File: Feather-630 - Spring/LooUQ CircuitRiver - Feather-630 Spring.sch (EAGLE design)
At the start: 22 parts, among them J1 FEATHERHOST-S, J2 FEATHERHOST-L, J3 HA-CTA_HEADER, J4 JST_PH-2_T/H, J5 JST_PH-2_T/H, P1 NO MOUNT, P2 NO MOUNT, P3 BREAKOUTPAD, U2 LM2674_BUCK

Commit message: Updates for Feather-630
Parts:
- removed P1, P2: NO MOUNT, common:BREAKOUTPAD
- added J6: QWIIC_VERTICAL, common:QWIIC_VERTICAL
- added J7: B8B-PH-K-S(LF)(SN), common:B8B-PH-K-S(LF)(SN)
- added J8: DNF, common:2PIN_T/H_HEADER
- J3: value HA-CTA_HEADER -> CR-SPRING_HEADER; device common:HA-CTA_HEADER -> common:CR-SPRING_HEADER
- P3: value BREAKOUTPAD -> SLEEP; device common:BREAKOUTPAD -> common:SLEEP
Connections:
- removed net Net_17: J2.+3V3, J2.AREF, P1.1, P2.1
- removed net Net_GND: C1.MINUS, C2.MINUS, C4.2, D1.A, J2.GND@2, J3.GND, J4.P2, J5.P2, R2.2, R3.1, U2.GND
- new net Net_11: J2.A0, J7.P8
- new net Net_23: J2.A3, J7.P5
- new net Net_24: J2.A2, J7.P6
- new net Net_25: J2.A1, J7.P7
- new net Net_27: J1.SDA, J6.SDA
- new net Net_28: J1.SCI, J6.SCL
- new net Net_29: J2.+3V3, J6.3v3, J8.P1
- new net Net_VIn: C1.PLUS, J5.P1, R1.2, U2.VIN
- net Net_13: now also C1.MINUS, C2.MINUS, C4.2, D1.A, J2.GND@2, J3.GND, J4.P2, J5.P2, J6.GND, J7.P2, J8.P2, R2.2, R3.1, U2.GND; no longer C1.PLUS, J5.P1, R1.2, U2.VIN
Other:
- note added: "D9 (aka A7) is tied to Adafruit's"
- note added: "Feather vbatt sense voltage divider"
- note added: "I/O"
- note added: "JST-PH DNF"
- note removed: "D9 (aka A7) is tied to Feather"
- note removed: "vbatt sense voltage divider"
- moved on the sheet: J1, J2

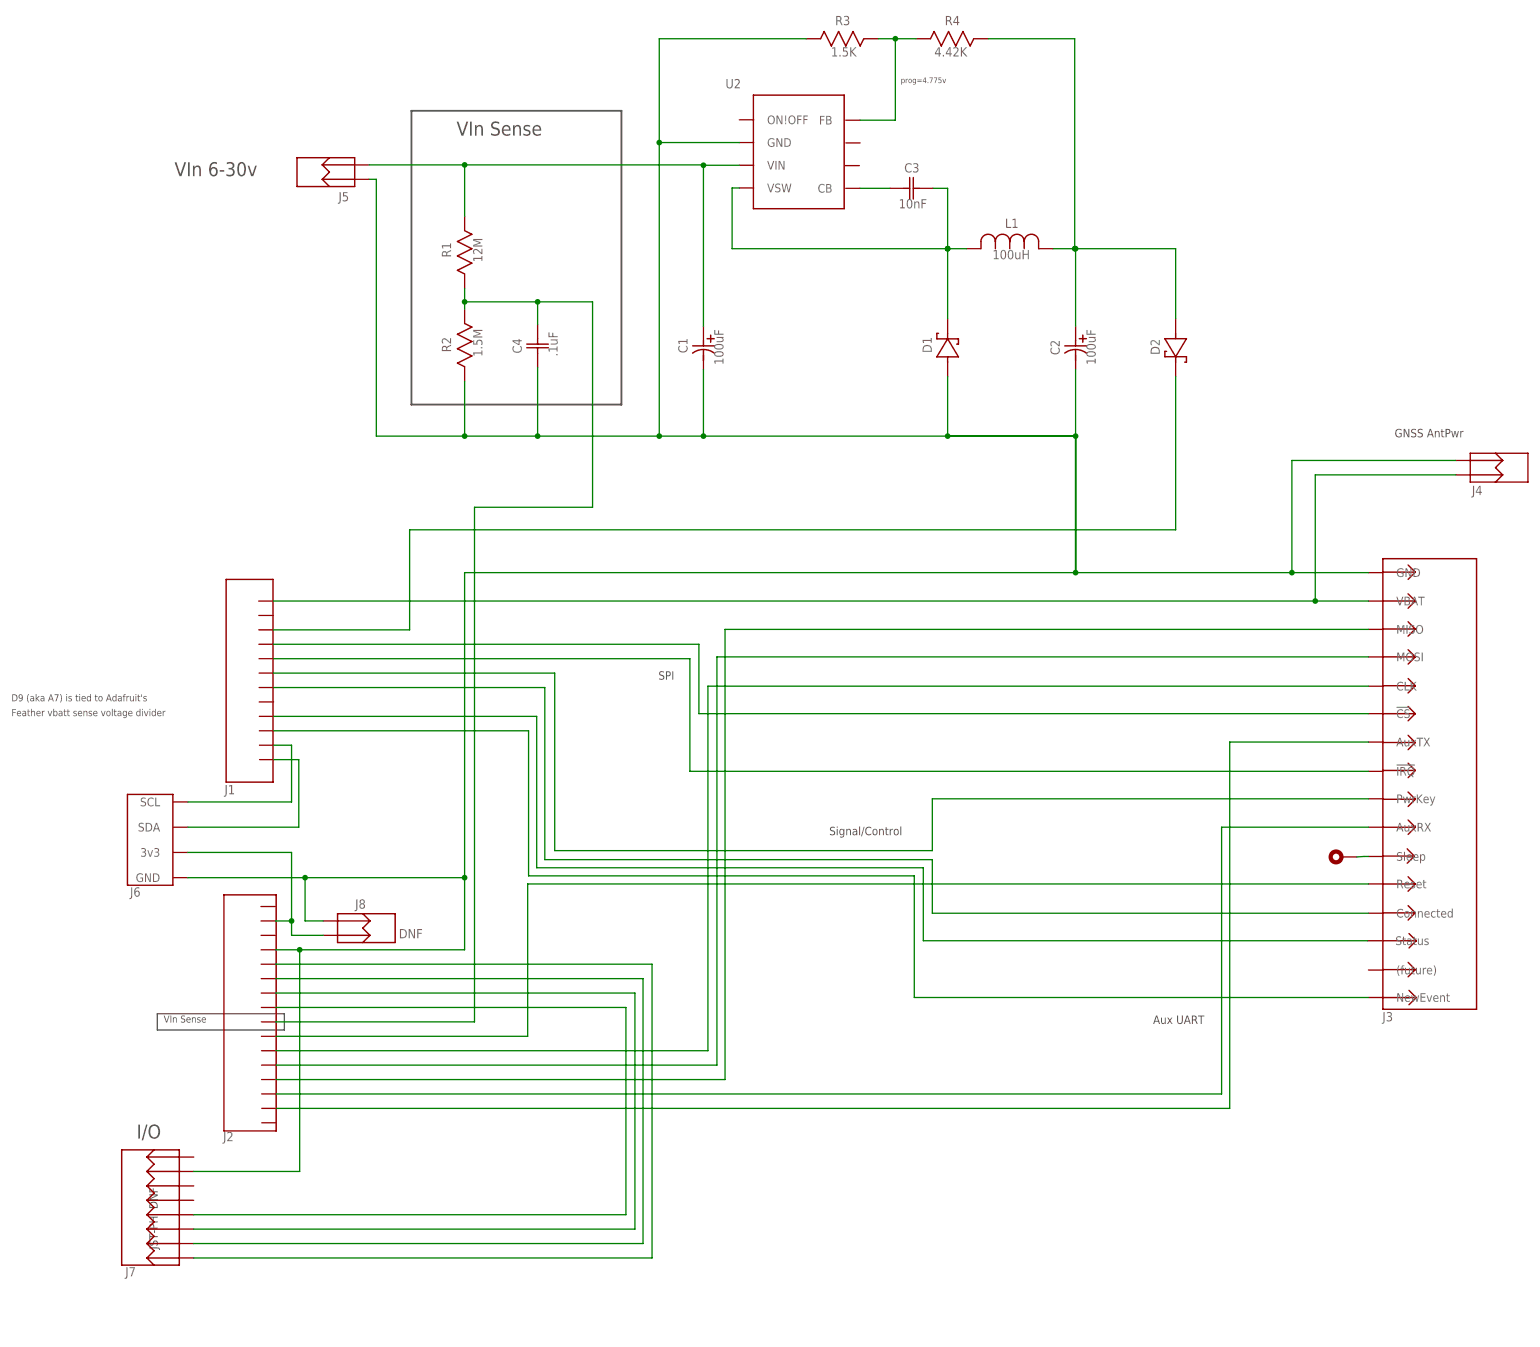
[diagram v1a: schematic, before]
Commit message: updated with CircuitRiver RapidsIO connector
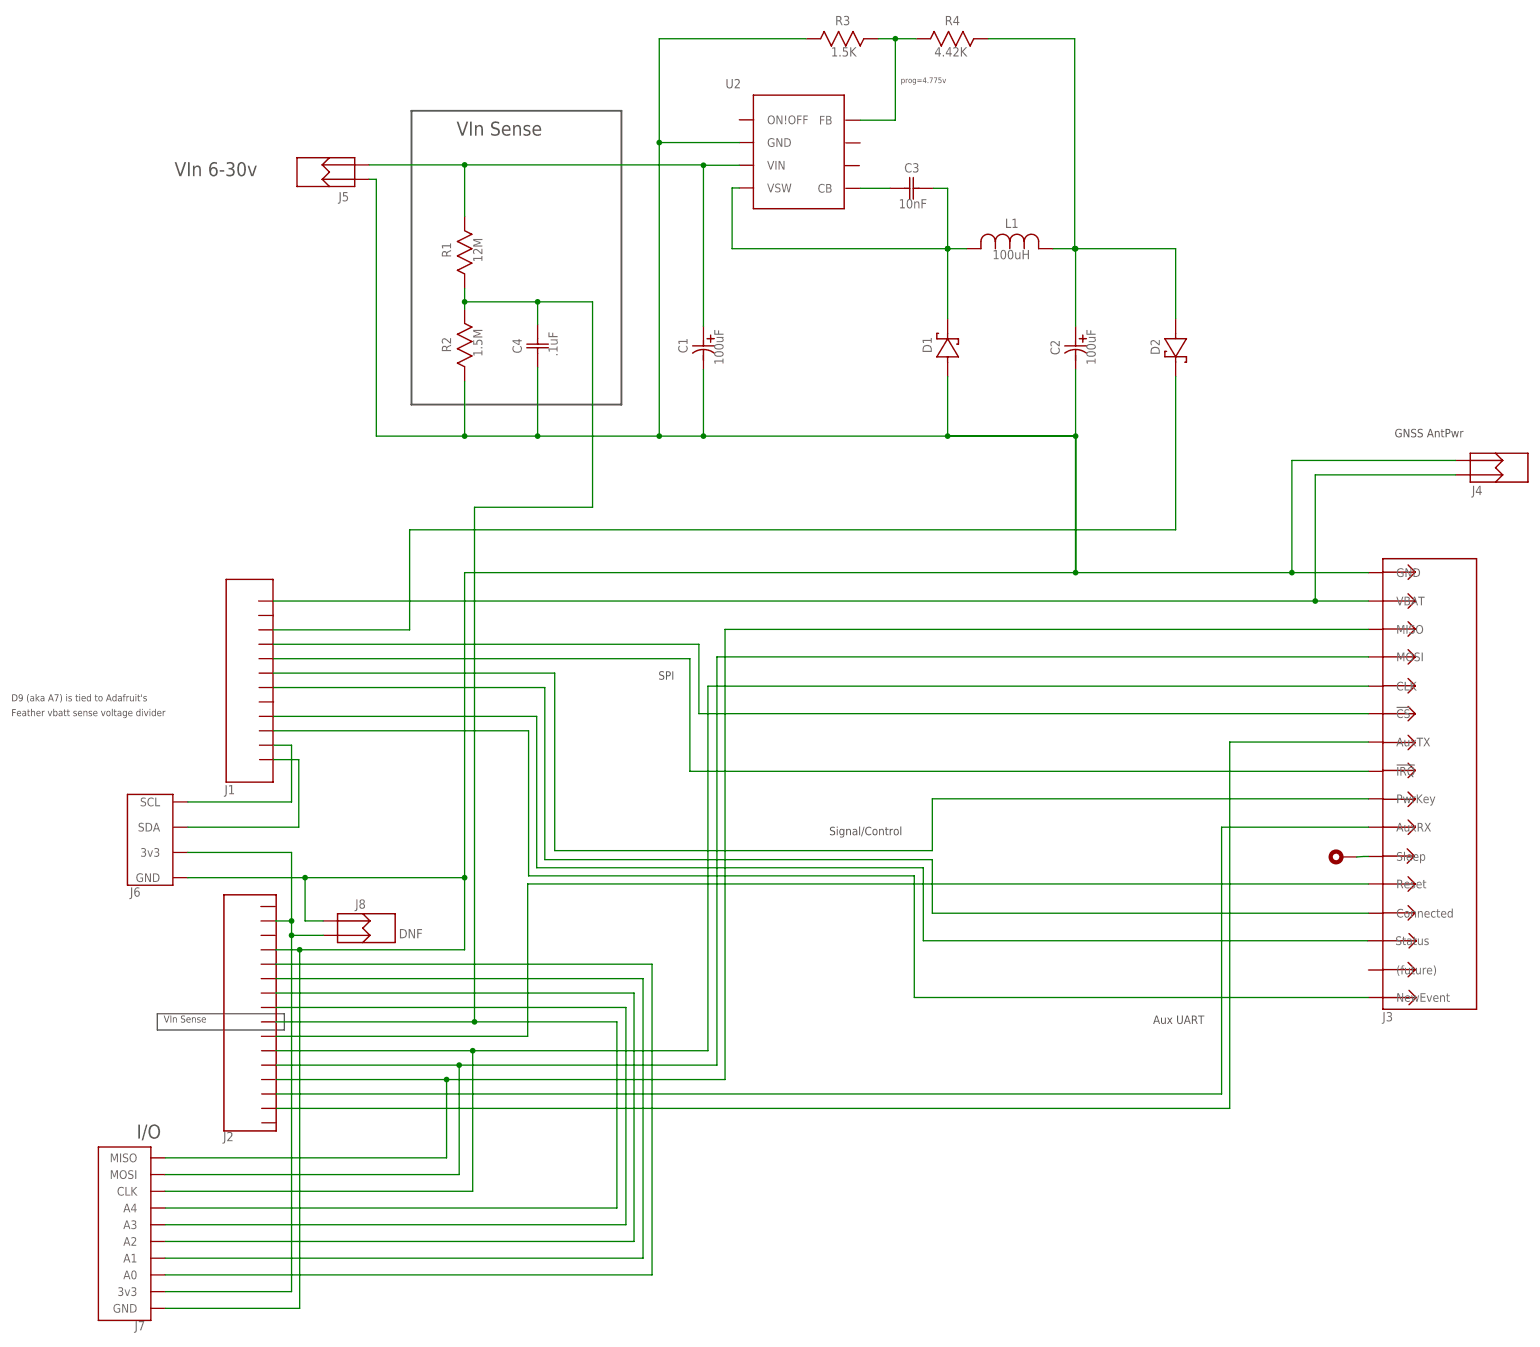
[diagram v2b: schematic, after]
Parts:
- J7: value B8B-PH-K-S(LF)(SN) -> CR-RAPIDSIO_VERTICAL; device common:B8B-PH-K-S(LF)(SN) -> common:CR-RAPIDSIO_VERTICAL
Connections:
- net Net_0 renamed Net_VBUS
- net Net_3 renamed Net_VSW
- removed net Net_13: C1.MINUS, C2.MINUS, C4.2, D1.A, J2.GND@2, J3.GND, J4.P2, J5.P2, J6.GND, J7.P2, J8.P2, R2.2, R3.1, U2.GND
- removed net Net_24: J2.A2, J7.P6
- removed net Net_29: J2.+3V3, J6.3v3, J8.P1
- new net Net_15: J2.A2, J7.A2
- new net Net_3v3: J2.+3V3, J6.3v3, J7.3v3, J8.P1
- new net Net_GND: C1.MINUS, C2.MINUS, C4.2, D1.A, J2.GND@2, J3.GND, J4.P2, J5.P2, J6.GND, J7.GND, J8.P2, R2.2, R3.1, U2.GND
- net Net_11: now also J7.A0; no longer J7.P8
- net Net_18: now also J7.A4
- net Net_2: now also J7.MISO
- net Net_23: now also J7.A3; no longer J7.P5
- net Net_25: now also J7.A1; no longer J7.P7
- net Net_6: now also J7.CLK
- net Net_8: now also J7.MOSI
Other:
- note removed: "JST-PH DNF"

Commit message: Updated Feathers
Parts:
- added P1, P2: DNF, common:DNF
- P3: value SLEEP -> DNF; device common:SLEEP -> common:DNF
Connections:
- new net Net_29: J2.AREF, J8.P1
- new net Net_30: J2.!RESET, P1.1
- net Net_3v3: now also J8.P2; no longer J8.P1
- net Net_GND: now also P2.1; no longer J8.P2
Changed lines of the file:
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@@
 <part name="LG1" library="common" deviceset="LOOUQ_LOGO" device=""/>
 <part name="LG2" library="common" deviceset="CIRCUITRIVER_LOGO" device=""/>
-<part name="P3" library="common" deviceset="SLEEP" device=""/>
+<part name="P1" library="common" deviceset="DNF" device=""/>
+<part name="P2" library="common" deviceset="DNF" device=""/>
+<part name="P3" library="common" deviceset="DNF" device=""/>
 <part name="R1" library="common" deviceset="RES_0603" device="" value="12M"/>
 <part name="R2" library="common" deviceset="RES_0603" device="" value="1.5M"/>
@@
 <instance part="LG1" gate="PART_1" x="114.776" y="131.128"/>
 <instance part="LG2" gate="PART_1" x="115.24" y="125.093"/>
+<instance part="P1" gate="BRKOUTPAD" x="-57.229" y="-13.176" rot="R90"/>
+<instance part="P2" gate="BRKOUTPAD" x="-57.071" y="-85.566" rot="R90"/>
 <instance part="P3" gate="BRKOUTPAD" x="101.362" y="-6.033" rot="R270"/>
 <instance part="R1" gate="PART_1" x="-52.223" y="100.477" rot="R90">
@@
 <busses/>
 <nets>
-<net name="Net_VBUS" class="1">
-<segment>
-<wire layer="91" width="0.25" x1="73.028" y1="78.581" x2="73.028" y2="51.594"/>
-<wire layer="91" width="0.25" x1="73.028" y1="51.594" x2="-61.913" y2="51.594"/>
-<wire layer="91" width="0.25" x1="-61.913" y1="51.594" x2="-61.913" y2="33.969"/>
-<wire layer="91" width="0.25" x1="-61.913" y1="33.969" x2="-85.94" y2="33.969"/>
-<pinref part="D2" gate="PART_1" pin="C"/>
-<pinref part="J1" gate="PART_1" pin="VBUS"/>
-</segment>
-</net>
 <net name="Net_1" class="0">
 <segment>
@@
 <pinref part="J7" gate="PART_1" pin="MISO"/>
 <junction x="-55.404" y="-45.248"/>
-</segment>
-</net>
-<net name="Net_VSW" class="1">
-<segment>
-<wire layer="91" width="0.25" x1="32.861" y1="88.741" x2="32.861" y2="101.113"/>
-<wire layer="91" width="0.25" x1="32.861" y1="101.113" x2="36.189" y2="101.113"/>
-<pinref part="D1" gate="PART_1" pin="C"/>
-<pinref part="L1" gate="PART_1" pin="1"/>
-<wire layer="91" width="0.25" x1="-5.106" y1="111.81" x2="-3.836" y2="111.81"/>
-<wire layer="91" width="0.25" x1="-5.106" y1="111.81" x2="-5.106" y2="101.113"/>
-<wire layer="91" width="0.25" x1="-5.106" y1="101.113" x2="32.861" y2="101.113"/>
-<pinref part="U2" gate="PART_1" pin="VSW"/>
-<junction x="32.861" y="101.113"/>
-<wire layer="91" width="0.25" x1="30.318" y1="111.748" x2="32.861" y2="111.748"/>
-<wire layer="91" width="0.25" x1="32.861" y1="111.748" x2="32.861" y2="101.113"/>
-<pinref part="C3" gate="PART_1" pin="2"/>
-<junction x="32.861" y="101.113"/>
 </segment>
 </net>
@@
 </segment>
 </net>
+<net name="Net_29" class="0">
+<segment>
+<wire layer="91" width="0.25" x1="-78.423" y1="-19.848" x2="-77.153" y2="-19.844"/>
+<wire layer="91" width="0.25" x1="-78.423" y1="-19.848" x2="-85.552" y2="-19.848"/>
+<pinref part="J8" gate="PART_1" pin="P1"/>
+<pinref part="J2" gate="PART_1" pin="AREF"/>
+</segment>
+</net>
+<net name="Net_30" class="0">
+<segment>
+<wire layer="91" width="0.25" x1="-60.801" y1="-13.176" x2="-80.804" y2="-13.176"/>
+<wire layer="91" width="0.25" x1="-80.804" y1="-13.176" x2="-80.804" y2="-14.768"/>
+<wire layer="91" width="0.25" x1="-80.804" y1="-14.768" x2="-85.573" y2="-14.768"/>
+<pinref part="P1" gate="BRKOUTPAD" pin="1"/>
+<pinref part="J2" gate="PART_1" pin="!RESET"/>
+</segment>
+</net>
 <net name="Net_3v3" class="1">
 <segment>
-<wire layer="91" width="0.25" x1="-77.153" y1="-19.844" x2="-82.709" y2="-19.844"/>
-<wire layer="91" width="0.25" x1="-82.709" y1="-19.844" x2="-82.709" y2="-17.308"/>
+<wire layer="91" width="0.25" x1="-100.965" y1="-5.239" x2="-82.709" y2="-5.239"/>
+<wire layer="91" width="0.25" x1="-82.709" y1="-17.304" x2="-82.709" y2="-17.308"/>
+<wire layer="91" width="0.25" x1="-82.709" y1="-5.239" x2="-82.709" y2="-17.304"/>
 <wire layer="91" width="0.25" x1="-82.709" y1="-17.308" x2="-85.563" y2="-17.308"/>
-<pinref part="J8" gate="PART_1" pin="P1"/>
+<pinref part="J6" gate="PART_1" pin="3v3"/>
 <pinref part="J2" gate="PART_1" pin="+3V3"/>
-<wire layer="91" width="0.25" x1="-100.965" y1="-5.239" x2="-82.709" y2="-5.239"/>
-<wire layer="91" width="0.25" x1="-82.709" y1="-5.239" x2="-82.709" y2="-17.308"/>
-<pinref part="J6" gate="PART_1" pin="3v3"/>
-<junction x="-82.709" y="-17.308"/>
-<wire layer="91" width="0.25" x1="-82.709" y1="-19.844" x2="-82.709" y2="-82.605"/>
+<wire layer="91" width="0.25" x1="-82.709" y1="-17.308" x2="-82.709" y2="-82.605"/>
 <wire layer="91" width="0.25" x1="-82.709" y1="-82.605" x2="-104.989" y2="-82.605"/>
 <pinref part="J7" gate="PART_1" pin="3v3"/>
-<junction x="-82.709" y="-19.844"/>
+<junction x="-82.709" y="-17.308"/>
+<wire layer="91" width="0.25" x1="-77.153" y1="-17.304" x2="-82.709" y2="-17.304"/>
+<pinref part="J8" gate="PART_1" pin="P2"/>
+<junction x="-82.709" y="-17.304"/>
 </segment>
 </net>
@@
 <pinref part="J4" gate="PART_1" pin="P2"/>
 <junction x="93.504" y="44.05"/>
-<wire layer="91" width="0.25" x1="-100.965" y1="-9.684" x2="-80.327" y2="-9.684"/>
-<wire layer="91" width="0.25" x1="-80.327" y1="-9.684" x2="-52.229" y2="-9.684"/>
+<wire layer="91" width="0.25" x1="-100.965" y1="-9.684" x2="-52.229" y2="-9.684"/>
 <pinref part="J6" gate="PART_1" pin="GND"/>
 <junction x="-52.229" y="-9.684"/>
-<wire layer="91" width="0.25" x1="-77.153" y1="-17.304" x2="-80.327" y2="-17.304"/>
-<wire layer="91" width="0.25" x1="-80.327" y1="-17.304" x2="-80.327" y2="-9.684"/>
-<pinref part="J8" gate="PART_1" pin="P2"/>
-<junction x="-80.327" y="-9.684"/>
 <wire layer="91" width="0.25" x1="-81.28" y1="-22.388" x2="-81.28" y2="-85.551"/>
 <wire layer="91" width="0.25" x1="-81.28" y1="-85.551" x2="-104.989" y2="-85.551"/>
 <pinref part="J7" gate="PART_1" pin="GND"/>
 <junction x="-81.28" y="-22.388"/>
+<wire layer="91" width="0.25" x1="-61.912" y1="-85.551" x2="-60.643" y2="-85.566"/>
+<wire layer="91" width="0.25" x1="-61.912" y1="-85.551" x2="-81.28" y2="-85.551"/>
+<pinref part="P2" gate="BRKOUTPAD" pin="1"/>
+<junction x="-81.28" y="-85.551"/>
 </segment>
 </net>
@@
 <pinref part="J4" gate="PART_1" pin="P1"/>
 <junction x="97.621" y="39.048"/>
+</segment>
+</net>
+<net name="Net_VBUS" class="1">
+<segment>
+<wire layer="91" width="0.25" x1="73.028" y1="78.581" x2="73.028" y2="51.594"/>
+<wire layer="91" width="0.25" x1="73.028" y1="51.594" x2="-61.913" y2="51.594"/>
+<wire layer="91" width="0.25" x1="-61.913" y1="51.594" x2="-61.913" y2="33.969"/>
+<wire layer="91" width="0.25" x1="-61.913" y1="33.969" x2="-85.94" y2="33.969"/>
+<pinref part="D2" gate="PART_1" pin="C"/>
+<pinref part="J1" gate="PART_1" pin="VBUS"/>
 </segment>
 </net>
@@
 </segment>
 </net>
+<net name="Net_VSW" class="1">
+<segment>
+<wire layer="91" width="0.25" x1="32.861" y1="88.741" x2="32.861" y2="101.113"/>
+<wire layer="91" width="0.25" x1="32.861" y1="101.113" x2="36.189" y2="101.113"/>
+<pinref part="D1" gate="PART_1" pin="C"/>
+<pinref part="L1" gate="PART_1" pin="1"/>
+<wire layer="91" width="0.25" x1="-5.106" y1="111.81" x2="-3.836" y2="111.81"/>
+<wire layer="91" width="0.25" x1="-5.106" y1="111.81" x2="-5.106" y2="101.113"/>
+<wire layer="91" width="0.25" x1="-5.106" y1="101.113" x2="32.861" y2="101.113"/>
+<pinref part="U2" gate="PART_1" pin="VSW"/>
+<junction x="32.861" y="101.113"/>
+<wire layer="91" width="0.25" x1="30.318" y1="111.748" x2="32.861" y2="111.748"/>
+<wire layer="91" width="0.25" x1="32.861" y1="111.748" x2="32.861" y2="101.113"/>
+<pinref part="C3" gate="PART_1" pin="2"/>
+<junction x="32.861" y="101.113"/>
+</segment>
+</net>
